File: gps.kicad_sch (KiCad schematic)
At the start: 17 parts, among them J5 SMA, U5 74LVC1G80, U6 ZOE-M8Q, Y1 32.768k

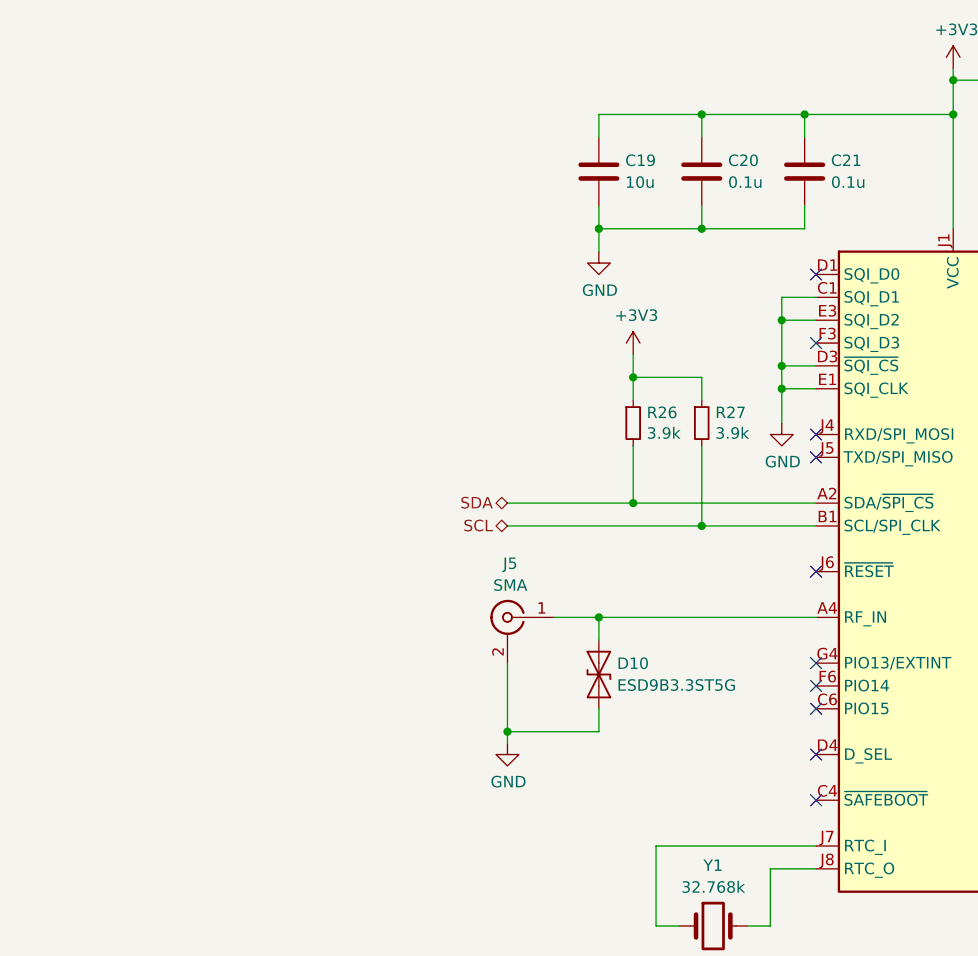
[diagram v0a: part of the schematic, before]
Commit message: added 4 inputs and 2 pwm outputs, completed routing
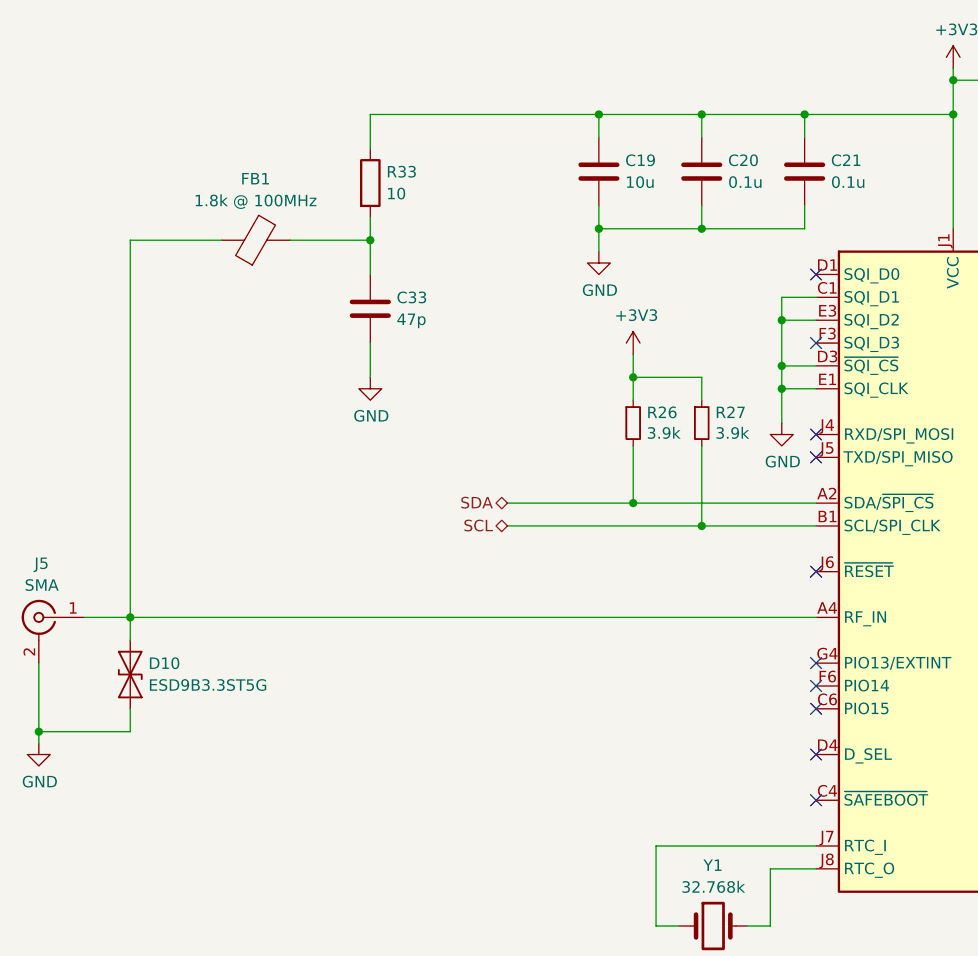
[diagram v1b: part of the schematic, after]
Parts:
- added C33: 47p, Capacitor_SMD:C_0603_1608Metric_Pad1.08x0.95mm_HandSolder, symbol Device:C
- added FB1: 1.8k @ 100MHz, Inductor_SMD:L_0402_1005Metric_Pad0.77x0.64mm_HandSolder, symbol Device:FerriteBead
- added R33: 10, Resistor_SMD:R_0603_1608Metric_Pad0.98x0.95mm_HandSolder, symbol Device:R
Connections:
- net +3V3: now also R33.1
- net GND: now also C33.2
- net at D10.2 (A2), J5.1 (In), U6.A4 (RF_IN): now also FB1.1
- new net: C33.1, FB1.2, R33.2
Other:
- moved on the sheet: D10, J5

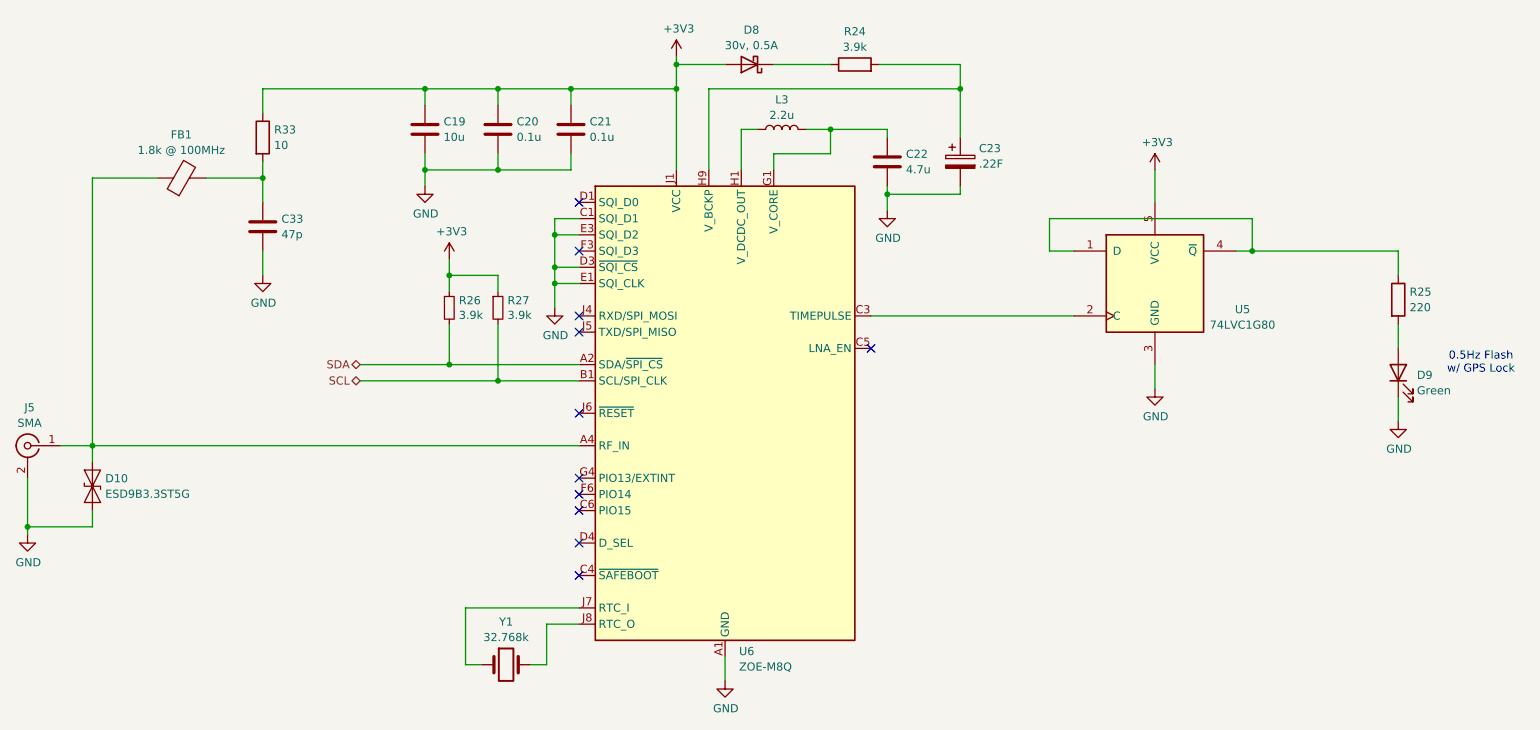
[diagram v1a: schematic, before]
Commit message: revised schematic after initial layout  - all connectors are vertical  - increased current handling of outputs  - replaced mechanical relay with ssr  - jumper to disable gps antenna power
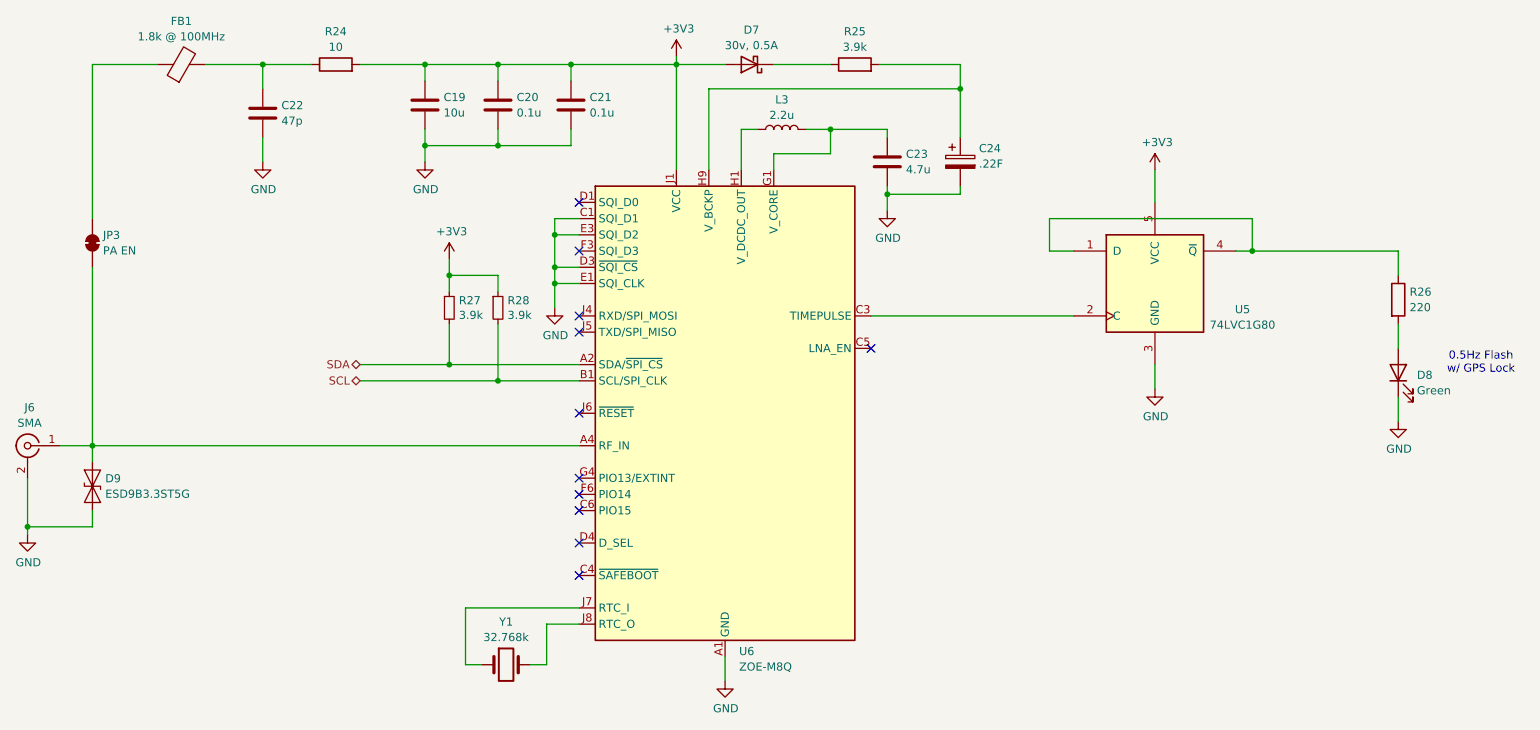
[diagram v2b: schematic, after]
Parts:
- added JP3: PA EN, Jumper:SolderJumper-2_P1.3mm_Open_RoundedPad1.0x1.5mm, symbol Jumper:SolderJumper_2_Bridged
- C19: footprint Capacitor_SMD:C_1206_3216Metric_Pad1.33x1.80mm_HandSolder -> Capacitor_SMD:C_1206_3216Metric
- C20, C21: footprint Capacitor_SMD:C_0603_1608Metric_Pad1.08x0.95mm_HandSolder -> Capacitor_SMD:C_0603_1608Metric
- C22: renamed from C33; footprint Capacitor_SMD:C_0603_1608Metric_Pad1.08x0.95mm_HandSolder -> Capacitor_SMD:C_0603_1608Metric
- C23: renamed from C22; footprint Capacitor_SMD:C_0603_1608Metric_Pad1.08x0.95mm_HandSolder -> Capacitor_SMD:C_0603_1608Metric
- D7: renamed from D8; footprint Diode_SMD:D_SOD-323_HandSoldering -> Diode_SMD:D_SOD-323
- D8: renamed from D9; footprint LED_SMD:LED_0603_1608Metric_Pad1.05x0.95mm_HandSolder -> LED_SMD:LED_0603_1608Metric
- FB1: footprint Inductor_SMD:L_0402_1005Metric_Pad0.77x0.64mm_HandSolder -> Inductor_SMD:L_0402_1005Metric
- L3: footprint Inductor_SMD:L_0805_2012Metric_Pad1.15x1.40mm_HandSolder -> Inductor_SMD:L_0805_2012Metric
- R24: renamed from R33; footprint Resistor_SMD:R_0603_1608Metric_Pad0.98x0.95mm_HandSolder -> Resistor_SMD:R_0603_1608Metric
- R25: renamed from R24; footprint Resistor_SMD:R_0603_1608Metric_Pad0.98x0.95mm_HandSolder -> Resistor_SMD:R_0603_1608Metric
- R26: renamed from R25; footprint Resistor_SMD:R_0603_1608Metric_Pad0.98x0.95mm_HandSolder -> Resistor_SMD:R_0603_1608Metric
- R27: renamed from R26; footprint Resistor_SMD:R_0603_1608Metric_Pad0.98x0.95mm_HandSolder -> Resistor_SMD:R_0603_1608Metric
- R28: renamed from R27; footprint Resistor_SMD:R_0603_1608Metric_Pad0.98x0.95mm_HandSolder -> Resistor_SMD:R_0603_1608Metric
- U5: footprint Package_TO_SOT_SMD:SOT-353_SC-70-5_Handsoldering -> Package_TO_SOT_SMD:SOT-353_SC-70-5
- Y1: footprint Crystal:Crystal_SMD_2012-2Pin_2.0x1.2mm_HandSoldering -> Crystal:Crystal_SMD_2012-2Pin_2.0x1.2mm
- renumbered C23 to C24, D10 to D9, J5 to J6
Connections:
- net +3V3: now also R24.2; no longer R24.1
- net at C22.1, FB1.2: now also R24.1; no longer R24.2
- net at D9.2 (A2), J6.1 (In), U6.A4 (RF_IN): now also JP3.1 (A); no longer FB1.1
- new net: FB1.1, JP3.2 (B)
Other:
- moved on the sheet: C19, C20, C21, C22, FB1, R24

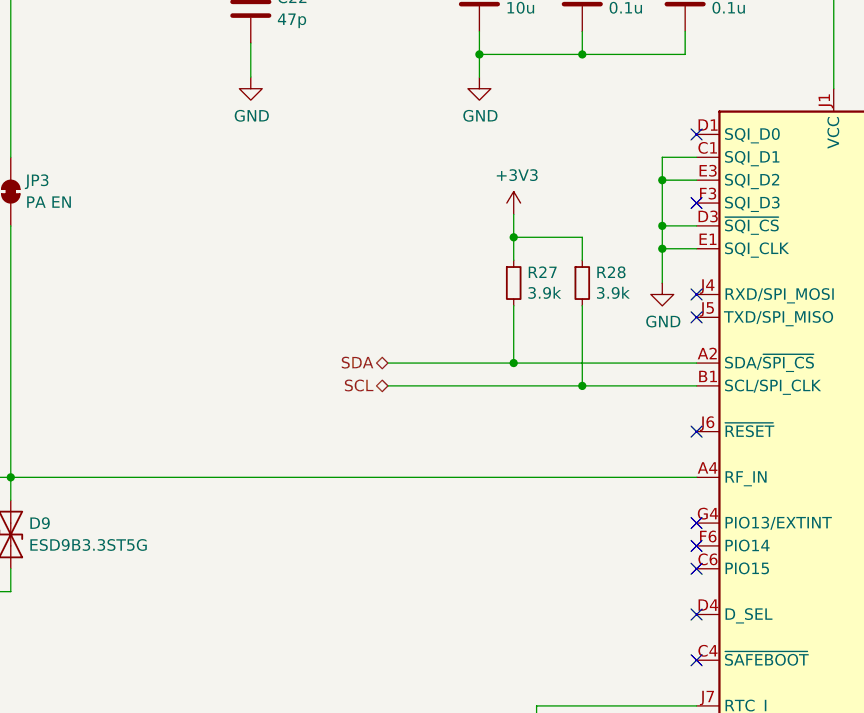
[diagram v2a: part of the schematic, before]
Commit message: add a version, add uart test pads to gps, sent for manufacturing
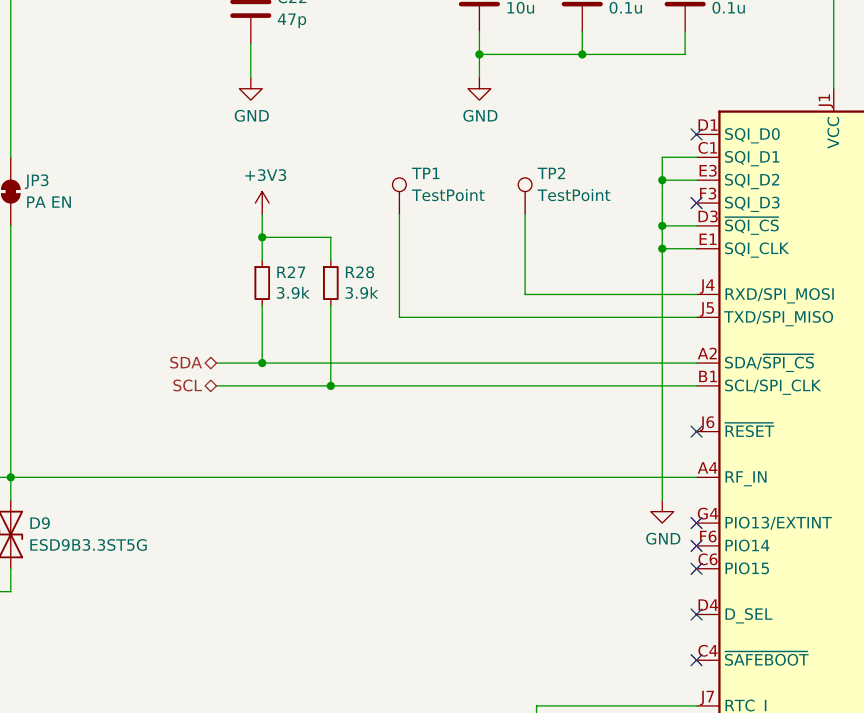
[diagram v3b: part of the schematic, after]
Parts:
- added TP1, TP2: TestPoint, TestPoint:TestPoint_Pad_1.0x1.0mm, symbol Connector:TestPoint
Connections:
- net at U6.J4 (RXD/SPI_MOSI): now also TP2.1
- net at U6.J5 (TXD/SPI_MISO): now also TP1.1
- no-connect marks 11 -> 9
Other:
- moved on the sheet: R27, R28

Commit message: filled in mfg part number for ordering
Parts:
- C22: Mfg Part Number (none) -> C0603C470K5RACAUTO
- JP3, TP1, TP2: Mfg Part Number (none) -> --
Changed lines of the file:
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@@
+			)
+		)
+		(property "Mfg Part Number" "--"
+			(at 86.36 80.01 0)
+			(effects
+				(font
+					(size 1.27 1.27)
+				)
+				(hide yes)
 			)
 		)
@@
 			)
 		)
+		(property "Mfg Part Number" "C0603C470K5RACAUTO"
+			(at 69.85 57.15 0)
+			(effects
+				(font
+					(size 1.27 1.27)
+				)
+				(hide yes)
+			)
+		)
 		(pin "2"
 		)
@@
 			)
 		)
+		(property "Mfg Part Number" "--"
+			(at 100.33 80.01 0)
+			(effects
+				(font
+					(size 1.27 1.27)
+				)
+				(hide yes)
+			)
+		)
 		(pin "1"
 		)
@@
 			(at 43.18 77.47 0)
 			(effects
+				(font
+					(size 1.27 1.27)
+				)
+				(hide yes)
+			)
+		)
+		(property "Mfg Part Number" "--"
+			(at 43.18 77.47 0)
+			(effects

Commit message: added missing 3d models, fussed with the silkscreen more
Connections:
- net at C22.1, R24.1: now also JP3.1 (A); no longer FB1.2
- net at D9.2 (A2), J6.1 (In), U6.A4 (RF_IN): now also FB1.1; no longer JP3.1 (A)
- net at JP3.2 (B): now also FB1.2; no longer FB1.1
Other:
- moved on the sheet: FB1, JP3
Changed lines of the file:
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@@
 	(symbol
 		(lib_id "Device:FerriteBead")
-		(at 57.15 49.53 90)
+		(at 43.18 77.47 180)
 		(unit 1)
 		(exclude_from_sim no)
@@
 		(fields_autoplaced yes)
 		(property "Reference" "FB1"
-			(at 57.0992 42.7439 90)
-			(effects
-				(font
-					(size 1.27 1.27)
-				)
+			(at 46.5836 76.3086 0)
+			(effects
+				(font
+					(size 1.27 1.27)
+				)
+				(justify right)
 			)
 		)
 		(property "Value" "1.8k @ 100MHz"
-			(at 57.0992 45.1682 90)
-			(effects
-				(font
-					(size 1.27 1.27)
-				)
+			(at 46.5836 78.7329 0)
+			(effects
+				(font
+					(size 1.27 1.27)
+				)
+				(justify right)
 			)
 		)
 		(property "Footprint" "Inductor_SMD:L_0402_1005Metric"
-			(at 57.15 51.308 90)
+			(at 44.958 77.47 90)
 			(effects
 				(font
@@
 		)
 		(property "Datasheet" "~"
-			(at 57.15 49.53 0)
+			(at 43.18 77.47 0)
 			(effects
 				(font
@@
 		)
 		(property "Description" "Ferrite bead"
-			(at 57.15 49.53 0)
+			(at 43.18 77.47 0)
 			(effects
 				(font
@@
 		)
 		(property "Mfg Part Number" "BLM15HD182SN1D"
-			(at 57.15 49.53 0)
+			(at 43.18 77.47 0)
 			(effects
 				(font
@@
 	(symbol
 		(lib_id "Jumper:SolderJumper_2_Bridged")
-		(at 43.18 77.47 90)
+		(at 57.15 49.53 180)
 		(unit 1)
 		(exclude_from_sim yes)
@@
 		(fields_autoplaced yes)
 		(property "Reference" "JP3"
-			(at 44.831 76.2578 90)
-			(effects
-				(font
-					(size 1.27 1.27)
-				)
-				(justify right)
+			(at 57.15 44.4965 0)
+			(effects
+				(font
+					(size 1.27 1.27)
+				)
 			)
 		)
 		(property "Value" "PA EN"
-			(at 44.831 78.6821 90)
-			(effects
-				(font
-					(size 1.27 1.27)
-				)
-				(justify right)
+			(at 57.15 46.9208 0)
+			(effects
+				(font
+					(size 1.27 1.27)
+				)
 			)
 		)
 		(property "Footprint" "Jumper:SolderJumper-2_P1.3mm_Open_RoundedPad1.0x1.5mm"
-			(at 43.18 77.47 0)
+			(at 57.15 49.53 0)
 			(effects
 				(font
@@
 		)
 		(property "Datasheet" "~"
-			(at 43.18 77.47 0)
+			(at 57.15 49.53 0)
 			(effects
 				(font
@@
 		)
 		(property "Description" "Solder Jumper, 2-pole, closed/bridged"
-			(at 43.18 77.47 0)
+			(at 57.15 49.53 0)
 			(effects
 				(font
@@
 		)
 		(property "Mfg Part Number" "--"
-			(at 43.18 77.47 0)
-			(effects
-				(font
+			(at 57.15 49.53 0)
+			(effects
+				(font

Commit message: bug fixes from testing
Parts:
- D7: footprint Diode_SMD:D_SOD-323 -> Custom:D_SOD-323HE
- L3: footprint Inductor_SMD:L_0805_2012Metric -> Custom:L_0806_2016Metric
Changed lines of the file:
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@@
 			)
 		)
-		(property "Footprint" "Inductor_SMD:L_0805_2012Metric"
+		(property "Footprint" "Custom:L_0806_2016Metric"
 			(at 151.13 59.69 0)
 			(effects
@@
 			)
 		)
-		(property "Footprint" "Diode_SMD:D_SOD-323"
+		(property "Footprint" "Custom:D_SOD-323HE"
 			(at 146.05 49.53 0)
 			(effects
